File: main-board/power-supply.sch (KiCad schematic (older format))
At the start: 21 parts, among them Q1 Q_NMOS_DGS, U2 AME40-12SMAZ, U3 LM7805

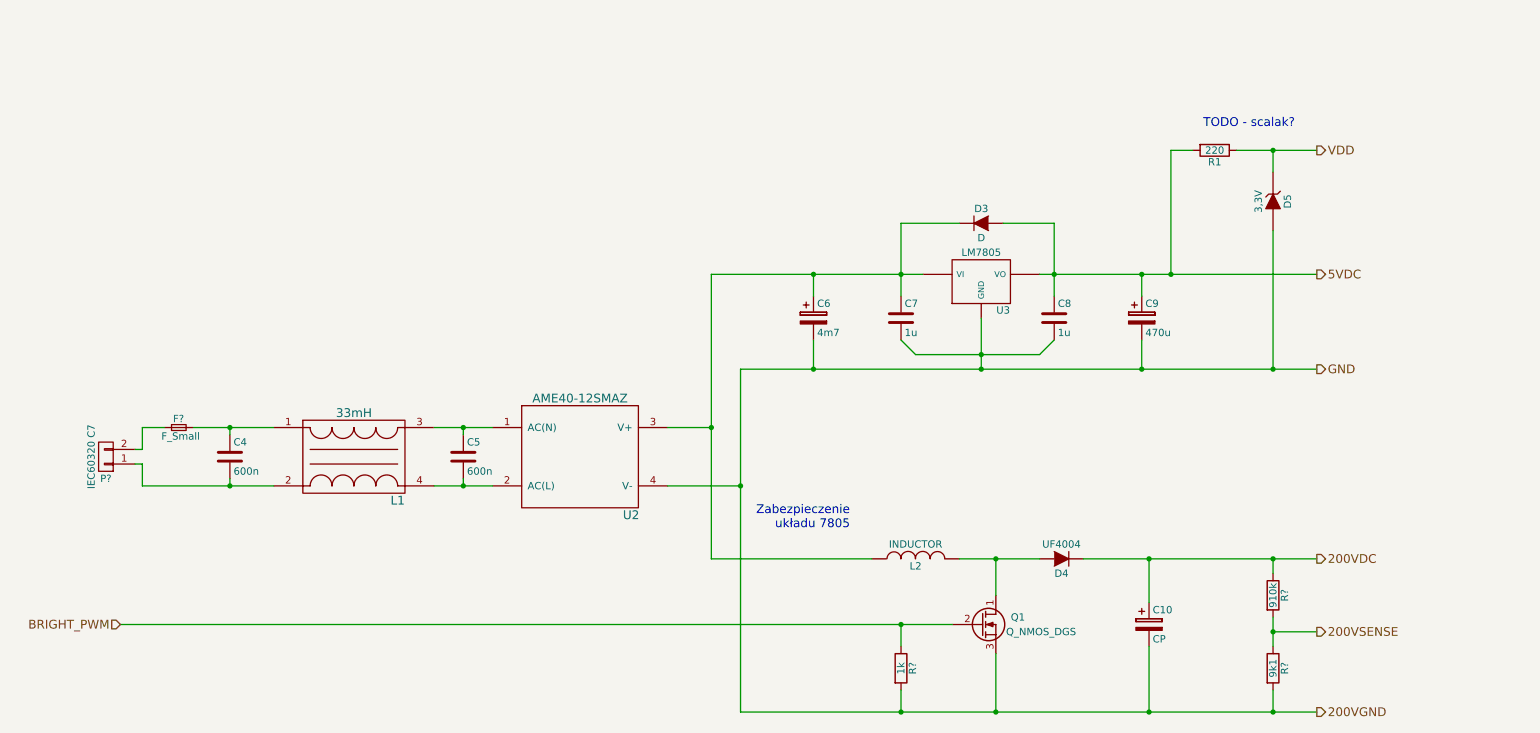
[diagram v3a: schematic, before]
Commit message: #1 - Przetwornica DC/DC 12V/5V
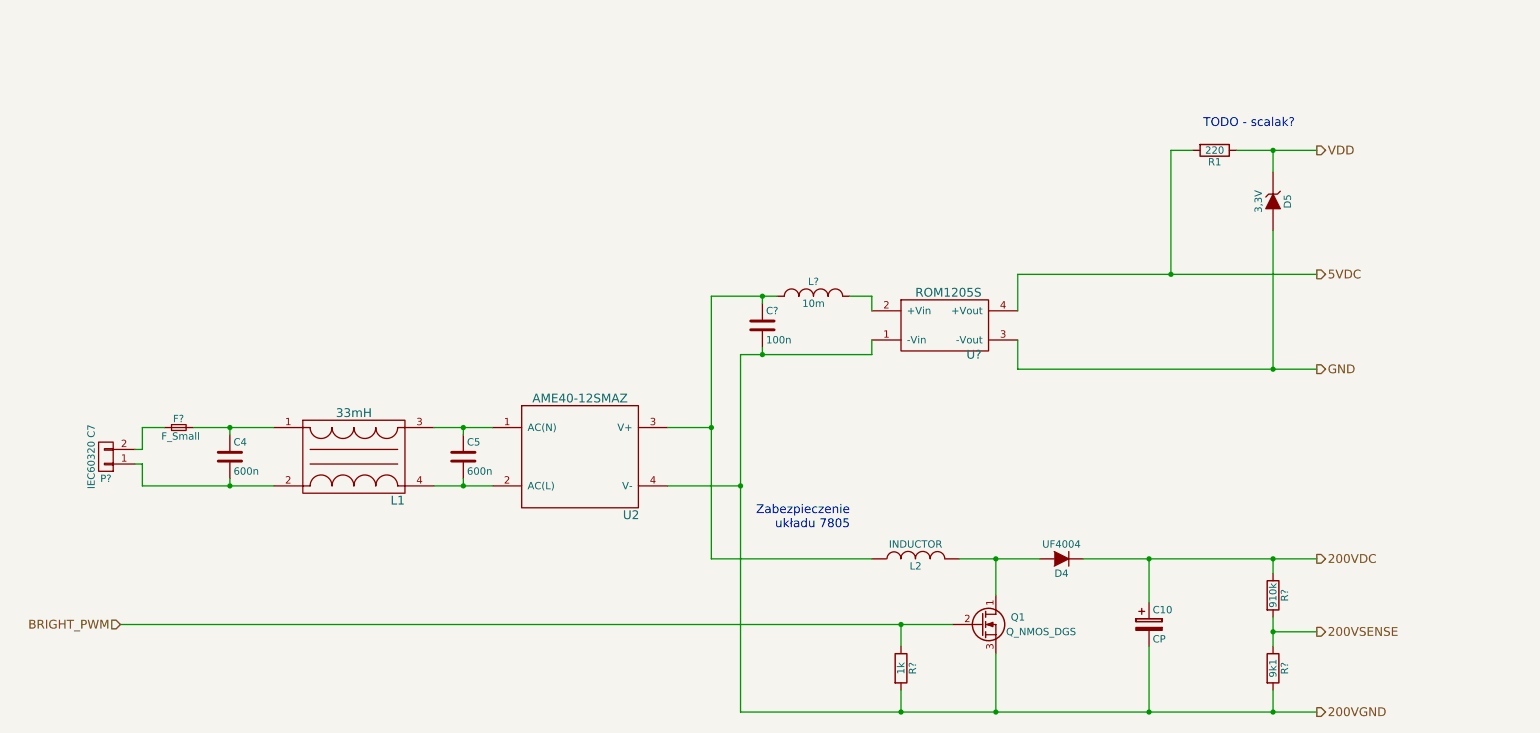
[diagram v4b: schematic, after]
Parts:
- removed C6: 4m7, symbol CP
- removed C7, C8: 1u, symbol C
- removed C9: 470u, symbol CP
- removed D3: D, symbol D
- removed U3: LM7805, symbol LM7805
- added C?: 100n, symbol C
- added L?: 10m, symbol INDUCTOR_SMALL
- added U?: ROM1205S, symbol ROM1205S
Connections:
- net 200VGND: now also C?.2, U?.1 (-Vin); no longer D5.2 (A)
- net 5VDC: now also U?.4 (+Vout)
- net at L2.1, U2.3 (V+): now also C?.1, L?.1
- new net: L?.2, U?.2 (+Vin)
- new net GND: D5.2 (A), U?.3 (-Vout)
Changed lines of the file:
@@
 Wire Wire Line
 	5000 3900 5500 3900
-$Comp
-L LM7805 U3
-U 1 1 581516AA
-P 7150 2500
-F 0 "U3" H 7300 2304 50  0000 C CNN
-F 1 "LM7805" H 7150 2700 50  0000 C CNN
-F 2 "" H 7150 2500 50  0000 C CNN
-F 3 "" H 7150 2500 50  0000 C CNN
-	1    7150 2500
-	1    0    0    -1
-$EndComp
-$Comp
-L CP C6
-U 1 1 58151831
-P 6000 2750
-F 0 "C6" H 6025 2850 50  0000 L CNN
-F 1 "4m7" H 6025 2650 50  0000 L CNN
-F 2 "" H 6038 2600 50  0000 C CNN
-F 3 "" H 6000 2750 50  0000 C CNN
-	1    6000 2750
-	1    0    0    -1
-$EndComp
-$Comp
-L CP C9
-U 1 1 581518E5
-P 8250 2750
-F 0 "C9" H 8275 2850 50  0000 L CNN
-F 1 "470u" H 8275 2650 50  0000 L CNN
-F 2 "" H 8288 2600 50  0000 C CNN
-F 3 "" H 8250 2750 50  0000 C CNN
-	1    8250 2750
-	1    0    0    -1
-$EndComp
-$Comp
-L C C7
-U 1 1 58151B4F
-P 6600 2750
-F 0 "C7" H 6625 2850 50  0000 L CNN
-F 1 "1u" H 6625 2650 50  0000 L CNN
-F 2 "" H 6638 2600 50  0000 C CNN
-F 3 "" H 6600 2750 50  0000 C CNN
-	1    6600 2750
-	1    0    0    -1
-$EndComp
-$Comp
-L C C8
-U 1 1 58151BB1
-P 7650 2750
-F 0 "C8" H 7675 2850 50  0000 L CNN
-F 1 "1u" H 7675 2650 50  0000 L CNN
-F 2 "" H 7688 2600 50  0000 C CNN
-F 3 "" H 7650 2750 50  0000 C CNN
-	1    7650 2750
-	1    0    0    -1
-$EndComp
-Wire Wire Line
-	6600 2100 6600 2600
-Wire Wire Line
-	5300 2450 6750 2450
-Wire Wire Line
-	6000 2600 6000 2450
-Connection ~ 6600 2450
-Wire Wire Line
-	7550 2450 9450 2450
-Wire Wire Line
-	7650 2100 7650 2600
-Wire Wire Line
-	8250 2450 8250 2600
-Connection ~ 7650 2450
-Connection ~ 8250 2450
-Wire Wire Line
-	6000 2900 6000 3100
-Wire Wire Line
-	5500 3100 9450 3100
-Wire Wire Line
-	7150 2750 7150 3100
-Connection ~ 7150 3100
-Wire Wire Line
-	8250 3100 8250 2900
-Connection ~ 8250 3100
-Wire Wire Line
-	6600 2900 6700 3000
-Wire Wire Line
-	6700 3000 7550 3000
-Connection ~ 7150 3000
-Wire Wire Line
-	7550 3000 7650 2900
-Wire Wire Line
-	5300 2450 5300 4400
-Connection ~ 6000 2450
-Wire Wire Line
-	5500 3100 5500 5450
-Connection ~ 6000 3100
+Wire Wire Line
+	5300 2600 5300 4400
+Wire Wire Line
+	5500 3000 5500 5450
 $Comp
 L INDUCTOR L2
@@
 	0    -1   -1   0
 $EndComp
-$Comp
-L D D3
-U 1 1 581539A7
-P 7150 2100
-F 0 "D3" H 7150 2200 50  0000 C CNN
-F 1 "D" H 7150 2000 50  0000 C CNN
-F 2 "" H 7150 2100 50  0000 C CNN
-F 3 "" H 7150 2100 50  0000 C CNN
-	1    7150 2100
-	1    0    0    -1
-$EndComp
-Wire Wire Line
-	7300 2100 7650 2100
-Wire Wire Line
-	7000 2100 6600 2100
 $Comp
 L Q_NMOS_DGS Q1
@@
 Wire Wire Line
 	1400 3650 1350 3650
+$Comp
+L ROM1205S U?
+U 1 1 582656C6
+P 6900 2800
+F 0 "U?" H 7100 2600 60  0000 C CNN
+F 1 "ROM1205S" H 6925 3025 60  0000 C CNN
+F 2 "" H 6800 2825 60  0001 C CNN
+F 3 "" H 6800 2825 60  0001 C CNN
+	1    6900 2800
+	1    0    0    -1
+$EndComp
+$Comp
+L INDUCTOR_SMALL L?
+U 1 1 5826597D
+P 6000 2600
+F 0 "L?" H 6000 2700 50  0000 C CNN
+F 1 "10m" H 6000 2550 50  0000 C CNN
+F 2 "" H 6000 2600 50  0000 C CNN
+F 3 "" H 6000 2600 50  0000 C CNN
+	1    6000 2600
+	1    0    0    -1
+$EndComp
+Wire Wire Line
+	5300 2600 5750 2600
+Wire Wire Line
+	5650 2600 5650 2650
+Connection ~ 5650 2600
+Wire Wire Line
+	6250 2600 6400 2600
+Wire Wire Line
+	6400 2600 6400 2700
+$Comp
+L C C?
+U 1 1 582658FD
+P 5650 2800
+F 0 "C?" H 5675 2900 50  0000 L CNN
+F 1 "100n" H 5675 2700 50  0000 L CNN
+F 2 "" H 5688 2650 50  0000 C CNN
+F 3 "" H 5650 2800 50  0000 C CNN
+	1    5650 2800
+	1    0    0    -1
+$EndComp
+Wire Wire Line
+	5500 3000 6400 3000
+Wire Wire Line
+	5650 3000 5650 2950
+Wire Wire Line
+	6400 3000 6400 2900
+Connection ~ 5650 3000
+Wire Wire Line
+	7400 2700 7400 2450
+Wire Wire Line
+	7400 2450 9450 2450
+Wire Wire Line
+	7400 2900 7400 3100
+Wire Wire Line
+	7400 3100 9450 3100
 $EndSCHEMATC

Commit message: #1 - dokumentacja ROM-1205S; usuniecie komentarza
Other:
- note removed: "Zabezpieczenie\nukładu 7805"
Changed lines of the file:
@@
 Wire Wire Line
 	5300 4400 6400 4400
-Text Notes 6250 4200 2    60   ~ 0
-Zabezpieczenie\nukładu 7805
 Text HLabel 9450 1600 2    60   Output ~ 0
 VDD
@@
 F 1 "ROM1205S" H 6925 3025 60  0000 C CNN
 F 2 "" H 6800 2825 60  0001 C CNN
-F 3 "" H 6800 2825 60  0001 C CNN
+F 3 "http://www.recom-power.com/pdf/Econoline/ROM.pdf" H 6800 2825 60  0001 C CNN
 	1    6900 2800
 	1    0    0    -1

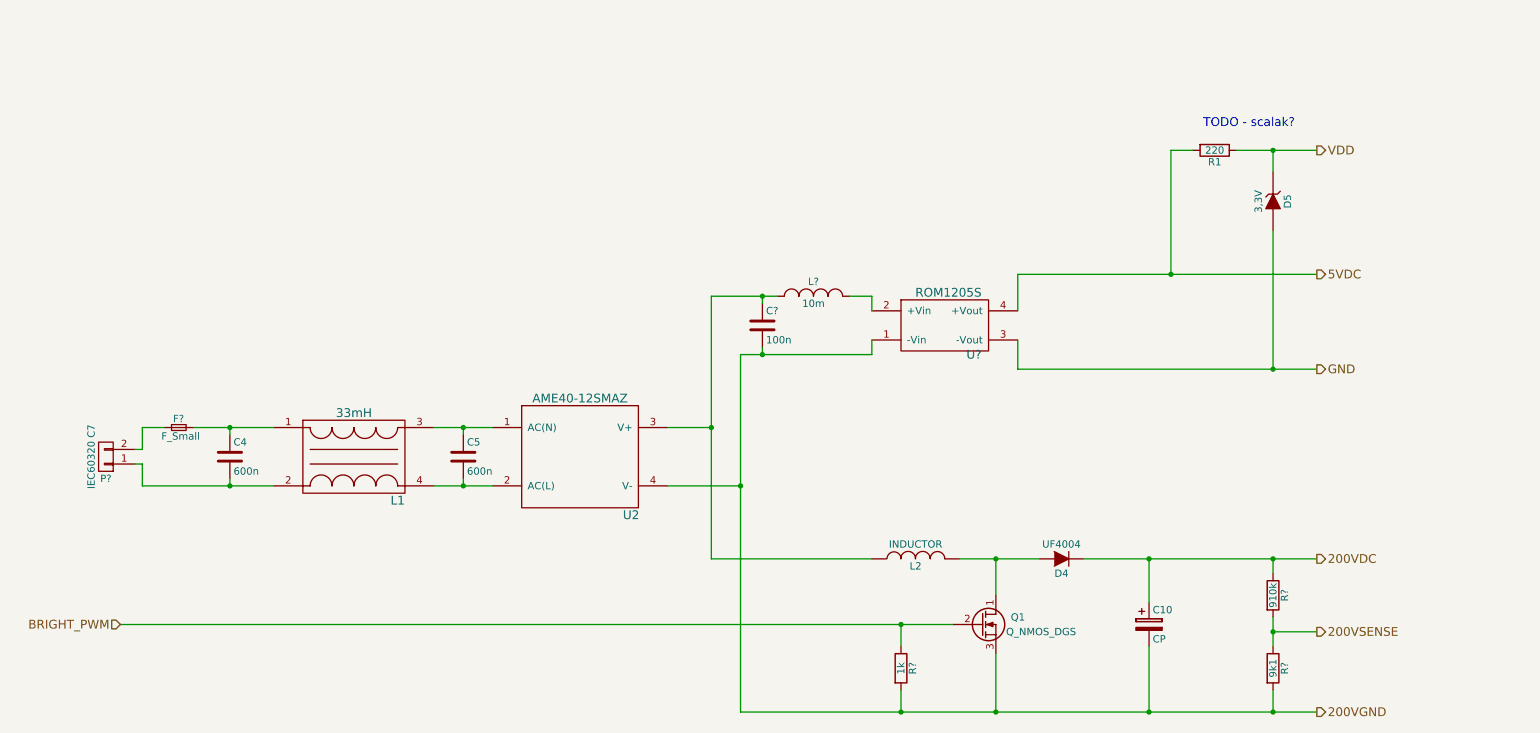
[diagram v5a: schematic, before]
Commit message: #1 - stabilizator LDO AMS1117-3.3V
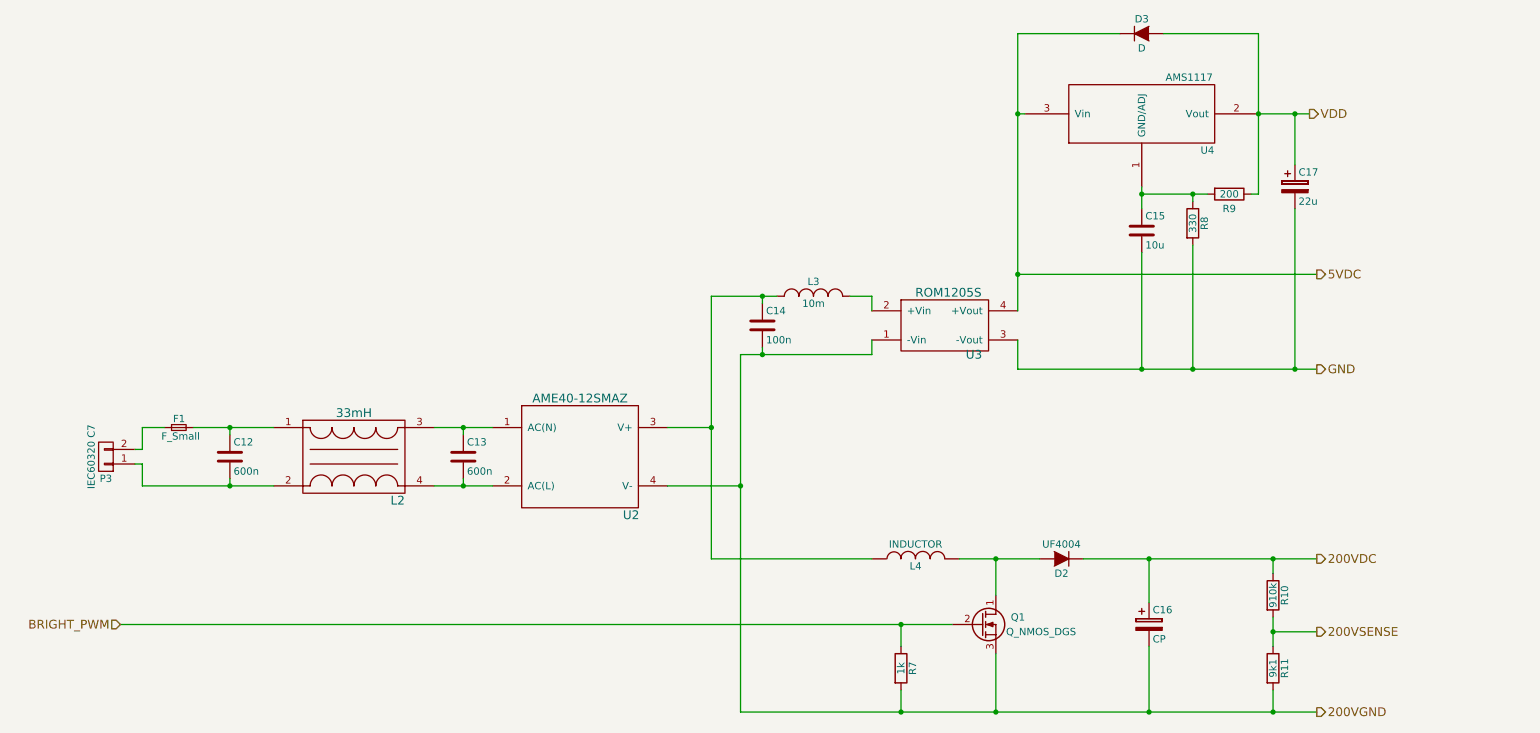
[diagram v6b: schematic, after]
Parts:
- removed D5: 3,3V, symbol ZENER
- removed R1: 220, symbol R
- added C15: 10u, symbol C
- added C17: 22u, symbol CP
- added D3: D, symbol D
- added R8: 330, symbol R
- added R9: 200, symbol R
- added U4: AMS1117, symbol AMS1117
- gave numbers to parts that had none: 8
- renumbered C4 to C12, C5 to C13, C10 to C16, D4 to D2, L1 to L2, L2 to L4
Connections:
- net 5VDC: now also D3.1 (K), U4.3 (Vin)
- net GND: now also C15.2, C17.2, R8.2
- net VDD: now also C17.1, D3.2 (A), R9.1, U4.2 (Vout)
- new net: C15.1, R8.1, R9.2, U4.1 (GND/ADJ)
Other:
- note removed: "TODO - scalak?"

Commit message: Niezapisane zmiany
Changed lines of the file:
@@
 $EndComp
 Wire Wire Line
-	3400 3500 3600 3500
-Wire Wire Line
-	3600 3500 3800 3500
-Wire Wire Line
-	3400 3900 3600 3900
-Wire Wire Line
-	3600 3900 3800 3900
+	3400 3500 3800 3500
+Wire Wire Line
+	3400 3900 3800 3900
 Wire Wire Line
 	3600 3900 3600 3850
@@
 $EndComp
 Wire Wire Line
-	1750 3500 2000 3500
-Wire Wire Line
-	2000 3500 2300 3500
+	1750 3500 2300 3500
 Wire Wire Line
 	2000 3500 2000 3550
@@
 	1400 3750 1400 3900
 Wire Wire Line
-	1400 3900 2000 3900
-Wire Wire Line
-	2000 3900 2300 3900
+	1400 3900 2300 3900
 Wire Wire Line
 	2000 3900 2000 3850
@@
 	5000 3900 5500 3900
 Wire Wire Line
-	5300 2600 5300 3500
-Wire Wire Line
-	5300 3500 5300 4400
-Wire Wire Line
-	5500 3000 5500 3900
-Wire Wire Line
-	5500 3900 5500 5450
+	5300 2600 5300 4400
+Wire Wire Line
+	5500 3000 5500 5450
 $Comp
 L INDUCTOR L4
@@
 $EndComp
 Wire Wire Line
-	7000 4400 7250 4400
-Wire Wire Line
-	7250 4400 7550 4400
+	7000 4400 7550 4400
 Wire Wire Line
 	7250 4400 7250 4650
 Connection ~ 7250 4400
 Wire Wire Line
-	7850 4400 8300 4400
-Wire Wire Line
-	8300 4400 9150 4400
-Wire Wire Line
-	9150 4400 9450 4400
+	7850 4400 9450 4400
 Wire Wire Line
 	8300 4400 8300 4700
@@
 	7250 5450 7250 5050
 Wire Wire Line
-	5500 5450 6600 5450
-Wire Wire Line
-	6600 5450 7250 5450
-Wire Wire Line
-	7250 5450 8300 5450
-Wire Wire Line
-	8300 5450 9150 5450
-Wire Wire Line
-	9150 5450 9450 5450
+	5500 5450 9450 5450
 Wire Wire Line
 	8300 5450 8300 5000
@@
 Connection ~ 5500 3900
 Wire Wire Line
-	1250 4850 6600 4850
-Wire Wire Line
-	6600 4850 6950 4850
+	1250 4850 6950 4850
 Wire Wire Line
 	5300 4400 6400 4400
@@
 Connection ~ 9150 4400
 Wire Wire Line
-	9150 4800 9150 4900
-Wire Wire Line
-	9150 4900 9150 5000
+	9150 4800 9150 5000
 Wire Wire Line
 	9150 5300 9150 5450
@@
 $EndComp
 Wire Wire Line
-	5300 2600 5650 2600
-Wire Wire Line
-	5650 2600 5750 2600
+	5300 2600 5750 2600
 Wire Wire Line
 	5650 2600 5650 2650
@@
 $EndComp
 Wire Wire Line
-	5500 3000 5650 3000
-Wire Wire Line
-	5650 3000 6400 3000
+	5500 3000 6400 3000
 Wire Wire Line
 	5650 3000 5650 2950
@@
 Connection ~ 5650 3000
 Wire Wire Line
-	7400 800  7400 1350
-Wire Wire Line
-	7400 1350 7400 2450
-Wire Wire Line
-	7400 2450 7400 2700
+	7400 800  7400 2700
 Wire Wire Line
 	7400 2450 9450 2450
@@
 	7400 2900 7400 3100
 Wire Wire Line
-	7400 3100 8250 3100
-Wire Wire Line
-	8250 3100 8600 3100
-Wire Wire Line
-	8600 3100 9300 3100
-Wire Wire Line
-	9300 3100 9450 3100
+	7400 3100 9450 3100
 Wire Wire Line
 	7450 1350 7400 1350
@@
 $EndComp
 Wire Wire Line
-	9050 800  9050 1350
-Wire Wire Line
-	9050 1350 9050 1900
+	9050 800  9050 1900
 Wire Wire Line
 	9050 800  8400 800
@@
 $EndComp
 Wire Wire Line
-	8250 1850 8250 1900
-Wire Wire Line
-	8250 1900 8250 2000
+	8250 1850 8250 2000
 Wire Wire Line
 	8250 2300 8250 3100
 Connection ~ 8250 3100
 Wire Wire Line
-	8700 1900 8600 1900
-Wire Wire Line
-	8600 1900 8250 1900
+	8250 1900 8700 1900
 Connection ~ 8250 1900
 Wire Wire Line
@@
 Connection ~ 9050 1350
 Wire Wire Line
-	9050 1350 9300 1350
-Wire Wire Line
-	9300 1350 9400 1350
+	9050 1350 9400 1350
 Wire Wire Line
 	9300 1350 9300 1700
